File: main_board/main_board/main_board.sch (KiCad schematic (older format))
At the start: 7 parts, among them J1 jstsh4x1, U1 Teensy3.5_All_Pins

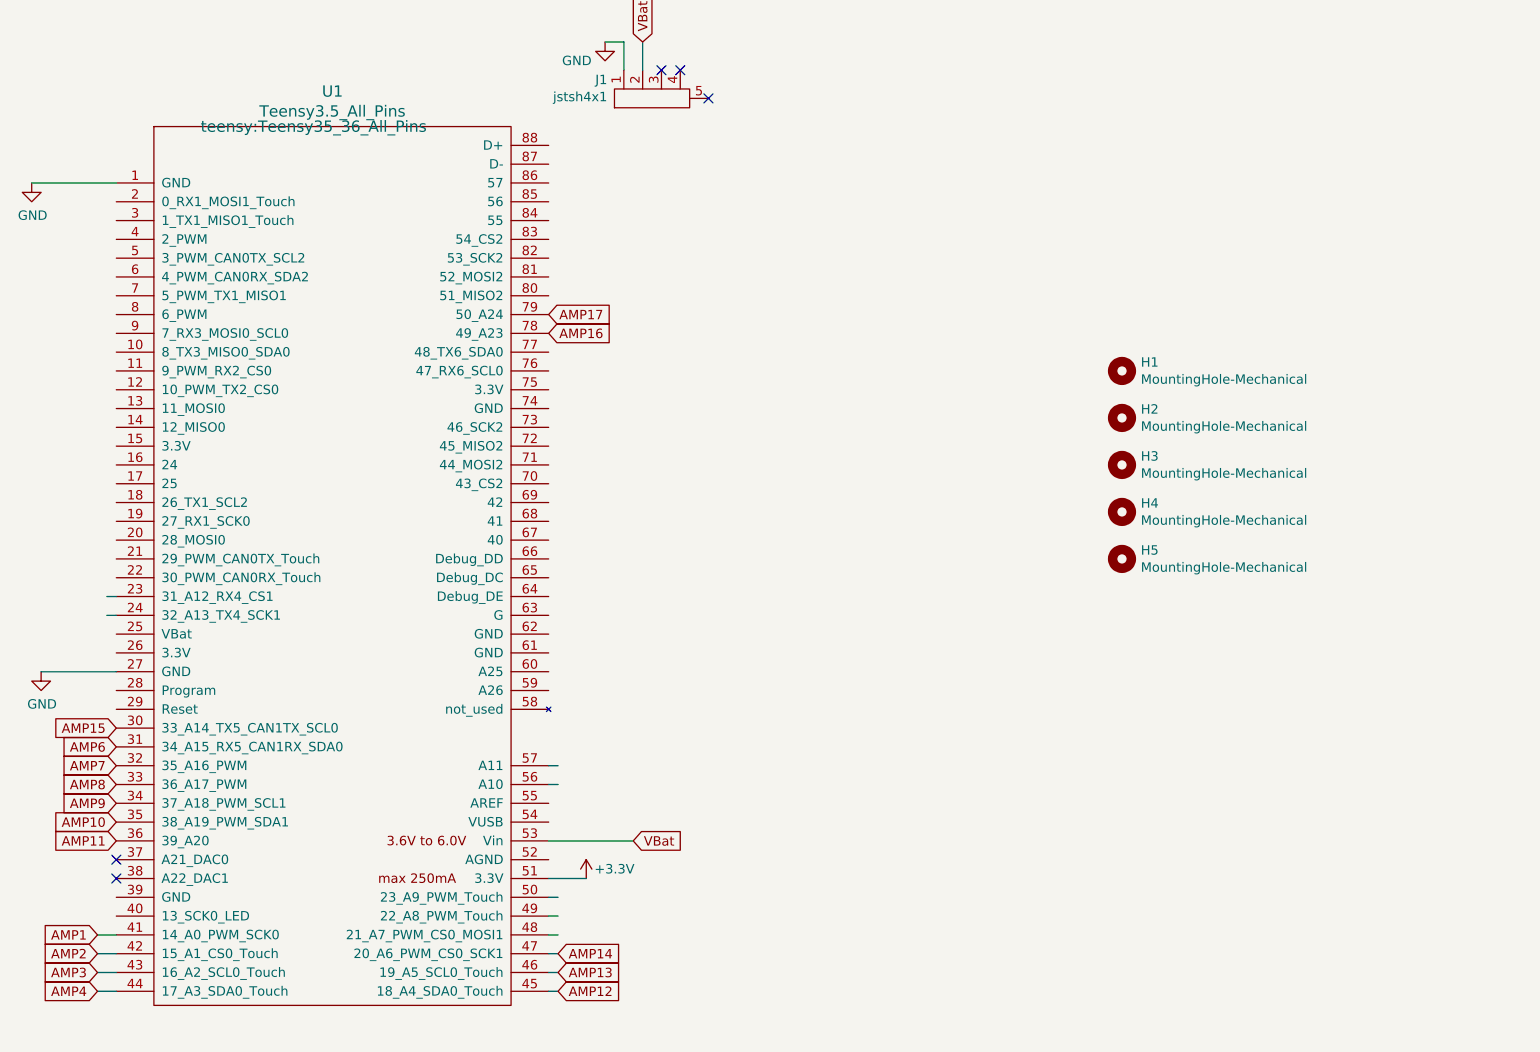
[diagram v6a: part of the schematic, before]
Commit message: fixed dogbones
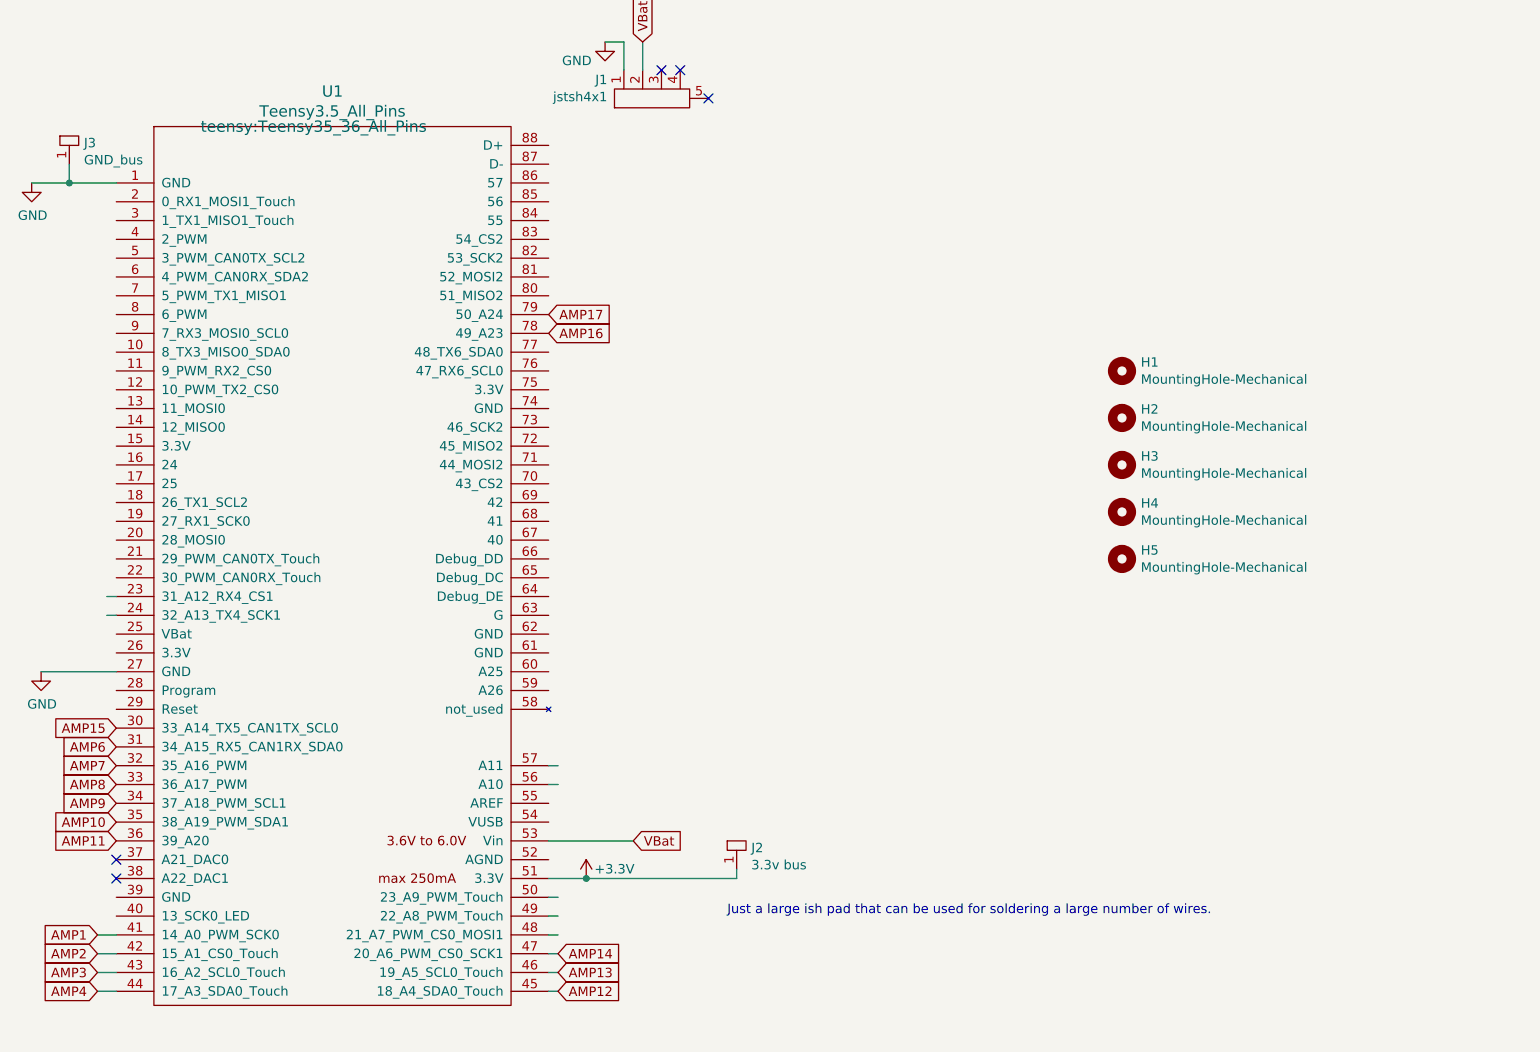
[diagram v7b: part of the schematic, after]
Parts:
- added J2: 3.3v bus, exocam_charge_amp:power_bus, symbol exocam_charge_amp:power_bus
- added J3: GND_bus, exocam_charge_amp:power_bus, symbol exocam_charge_amp:power_bus
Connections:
- wire segments 21 -> 25
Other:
- note added: "Just a large ish pad that can be used for soldering a large number of wires."
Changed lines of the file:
@@
 $EndComp
 Wire Wire Line
-	1000 1600 1450 1600
+	1000 1600 1200 1600
 $Comp
 L exocam_charge_amp-rescue:MountingHole-Mechanical H1
@@
 Text GLabel 1450 4500 0    50   Input ~ 0
 AMP15
+$Comp
+L exocam_charge_amp:power_bus J2
+U 1 1 610BF40F
+P 4750 5050
+F 0 "J2" H 4828 4963 50  0000 L CNN
+F 1 "3.3v bus" H 4828 4872 50  0000 L CNN
+F 2 "exocam_charge_amp:power_bus" H 4750 5050 50  0001 C CNN
+F 3 "" H 4750 5050 50  0001 C CNN
+	1    4750 5050
+	1    0    0    -1
+$EndComp
+Wire Wire Line
+	3950 5300 4750 5300
+Wire Wire Line
+	4750 5300 4750 5250
+Connection ~ 3950 5300
+$Comp
+L exocam_charge_amp:power_bus J3
+U 1 1 610C1AF2
+P 1200 1300
+F 0 "J3" H 1278 1213 50  0000 L CNN
+F 1 "GND_bus" H 1278 1122 50  0000 L CNN
+F 2 "exocam_charge_amp:power_bus" H 1200 1300 50  0001 C CNN
+F 3 "" H 1200 1300 50  0001 C CNN
+	1    1200 1300
+	1    0    0    -1
+$EndComp
+Wire Wire Line
+	1200 1600 1200 1500
+Connection ~ 1200 1600
+Wire Wire Line
+	1200 1600 1450 1600
+Text Notes 4700 5500 0    50   ~ 0
+Just a large ish pad that can be used for soldering a large number of wires.
 $EndSCHEMATC

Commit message: updated daughter board schematic
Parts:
- H1, H2, H3, H4, H5: symbol exocam_charge_amp-rescue:MountingHole-Mechanical -> main_board-rescue:MountingHole-Mechanical-exocam_charge_amp-rescue
- J1: symbol exocam_charge_amp:jstsh4x1 -> main_board-rescue:jstsh4x1-exocam_charge_amp
- J2, J3: symbol exocam_charge_amp:power_bus -> main_board-rescue:power_bus-exocam_charge_amp
- U1: symbol teensy:Teensy3.5_All_Pins -> main_board-rescue:Teensy3.5_All_Pins-teensy
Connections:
- net labels added: BAT, RTCBat
- net labels removed: VBat
- wire segments 25 -> 31
- no-connect marks 5 -> 3
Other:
- moved on the sheet: J2
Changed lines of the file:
@@
 $EndDescr
 $Comp
-L teensy:Teensy3.5_All_Pins U1
+L main_board-rescue:Teensy3.5_All_Pins-teensy U1
 U 1 1 60EFC6FB
 P 2600 3750
@@
 $EndSheet
 $Comp
-L exocam_charge_amp-cache:+3.3V #PWR0113
+L main_board-rescue:+3.3V-exocam_charge_amp-cache #PWR0113
 U 1 1 60F77ECF
-P 3950 5300
-F 0 "#PWR0113" H 3950 5150 50  0001 C CNN
-F 1 "+3.3V" H 4100 5350 50  0000 C CNN
-F 2 "" H 3950 5300 50  0001 C CNN
-F 3 "" H 3950 5300 50  0001 C CNN
-	1    3950 5300
+P 4750 5250
+F 0 "#PWR0113" H 4750 5100 50  0001 C CNN
+F 1 "+3.3V" H 4900 5300 50  0000 C CNN
+F 2 "" H 4750 5250 50  0001 C CNN
+F 3 "" H 4750 5250 50  0001 C CNN
+	1    4750 5250
 	1    0    0    -1
 $EndComp
@@
 	1000 1600 1200 1600
 $Comp
-L exocam_charge_amp-rescue:MountingHole-Mechanical H1
+L main_board-rescue:MountingHole-Mechanical-exocam_charge_amp-rescue H1
 U 1 1 60F7FB22
 P 6800 2600
@@
 $EndComp
 $Comp
-L exocam_charge_amp-rescue:MountingHole-Mechanical H2
+L main_board-rescue:MountingHole-Mechanical-exocam_charge_amp-rescue H2
 U 1 1 60F875E4
 P 6800 2850
@@
 $EndComp
 $Comp
-L exocam_charge_amp-rescue:MountingHole-Mechanical H3
+L main_board-rescue:MountingHole-Mechanical-exocam_charge_amp-rescue H3
 U 1 1 60F8850D
 P 6800 3100
@@
 $EndComp
 $Comp
-L exocam_charge_amp-rescue:MountingHole-Mechanical H4
+L main_board-rescue:MountingHole-Mechanical-exocam_charge_amp-rescue H4
 U 1 1 60F8942D
 P 6800 3350
@@
 Wire Wire Line
 	1400 3900 1450 3900
-$Comp
-L exocam_charge_amp:jstsh4x1 J1
-U 1 1 6111A17F
-P 4100 1100
-F 0 "J1" V 4149 1138 50  0000 L CNN
-F 1 "jstsh4x1" V 4058 1138 50  0000 L CNN
-F 2 "exocam_charge_amp:jstsh4x1" H 4050 1250 50  0001 C CNN
-F 3 "" H 4050 1250 50  0001 C CNN
-	1    4100 1100
-	0    -1   -1   0
-$EndComp
-Text GLabel 4250 850  1    50   Input ~ 0
-VBat
-Wire Wire Line
-	4250 850  4250 1000
+Text GLabel 4450 850  1    50   Input ~ 0
+RTCBat
 Wire Wire Line
 	4150 1000 4150 850
@@
 	1    0    0    -1
 $EndComp
-NoConn ~ 4350 1000
-NoConn ~ 4450 1000
 NoConn ~ 4600 1150
 Text GLabel 4200 5100 2    50   Input ~ 0
-VBat
+BAT
 Wire Wire Line
 	4200 5100 3750 5100
 $Comp
-L exocam_charge_amp-rescue:MountingHole-Mechanical H5
+L main_board-rescue:MountingHole-Mechanical-exocam_charge_amp-rescue H5
 U 1 1 61037EA1
 P 6800 3600
@@
 AMP15
 $Comp
-L exocam_charge_amp:power_bus J2
+L main_board-rescue:power_bus-exocam_charge_amp J2
 U 1 1 610BF40F
-P 4750 5050
-F 0 "J2" H 4828 4963 50  0000 L CNN
-F 1 "3.3v bus" H 4828 4872 50  0000 L CNN
-F 2 "exocam_charge_amp:power_bus" H 4750 5050 50  0001 C CNN
-F 3 "" H 4750 5050 50  0001 C CNN
-	1    4750 5050
-	1    0    0    -1
-$EndComp
-Wire Wire Line
-	3950 5300 4750 5300
+P 4500 5100
+F 0 "J2" H 4578 5013 50  0000 L CNN
+F 1 "3.3v bus" H 4578 4922 50  0000 L CNN
+F 2 "exocam_charge_amp:power_bus" H 4500 5100 50  0001 C CNN
+F 3 "" H 4500 5100 50  0001 C CNN
+	1    4500 5100
+	1    0    0    -1
+$EndComp
+Wire Wire Line
+	3950 5300 4500 5300
 Wire Wire Line
 	4750 5300 4750 5250
 Connection ~ 3950 5300
 $Comp
-L exocam_charge_amp:power_bus J3
+L main_board-rescue:power_bus-exocam_charge_amp J3
 U 1 1 610C1AF2
 P 1200 1300
@@
 Text Notes 4700 5500 0    50   ~ 0
 Just a large ish pad that can be used for soldering a large number of wires.
+$Comp
+L main_board-rescue:jstsh4x1-exocam_charge_amp J1
+U 1 1 6111A17F
+P 4100 1100
+F 0 "J1" V 4149 1138 50  0000 L CNN
+F 1 "jstsh4x1" V 4058 1138 50  0000 L CNN
+F 2 "exocam_charge_amp:jstsh4x1" H 4050 1250 50  0001 C CNN
+F 3 "" H 4050 1250 50  0001 C CNN
+	1    4100 1100
+	0    -1   -1   0
+$EndComp
+Wire Wire Line
+	4450 850  4450 1000
+Wire Wire Line
+	4350 1000 4350 800
+Wire Wire Line
+	4350 800  4150 800
+Wire Wire Line
+	4150 800  4150 850
+Connection ~ 4150 850
+Text GLabel 4250 850  1    50   Input ~ 0
+BAT
+Wire Wire Line
+	4250 850  4250 1000
+Text GLabel 1200 4000 0    50   Input ~ 0
+RTCBat
+Wire Wire Line
+	1200 4000 1450 4000
+Connection ~ 4500 5300
+Wire Wire Line
+	4500 5300 4750 5300
 $EndSCHEMATC
